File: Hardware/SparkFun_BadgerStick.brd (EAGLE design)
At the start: 17.8 x 66 mm, 39 parts, among them Q1 DMG2307L, U1 MIC5205-3.3V, U2 ATMEGA328P_TQFP, U3 CY7C65213, Y1 4MHz

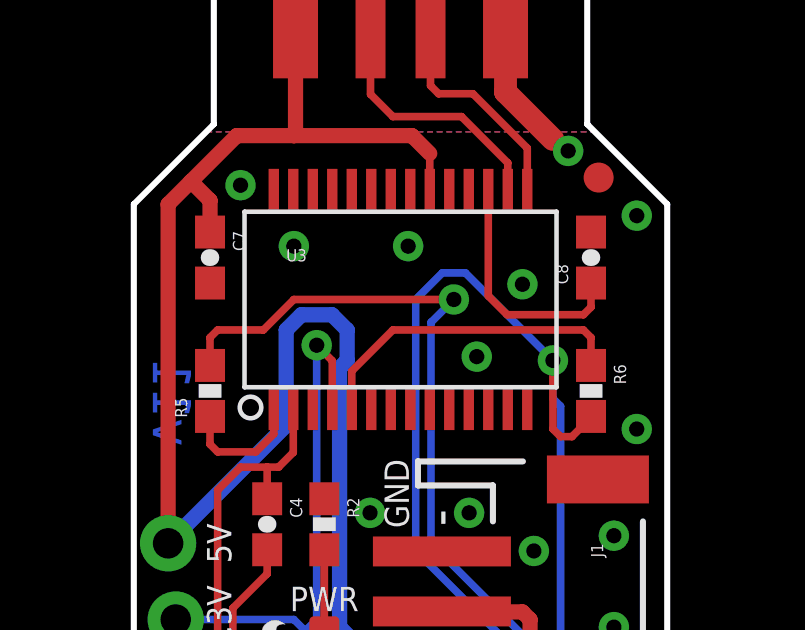
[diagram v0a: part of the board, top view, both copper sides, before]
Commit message: Switched Cypress USB-Serial bridge to FT232RL
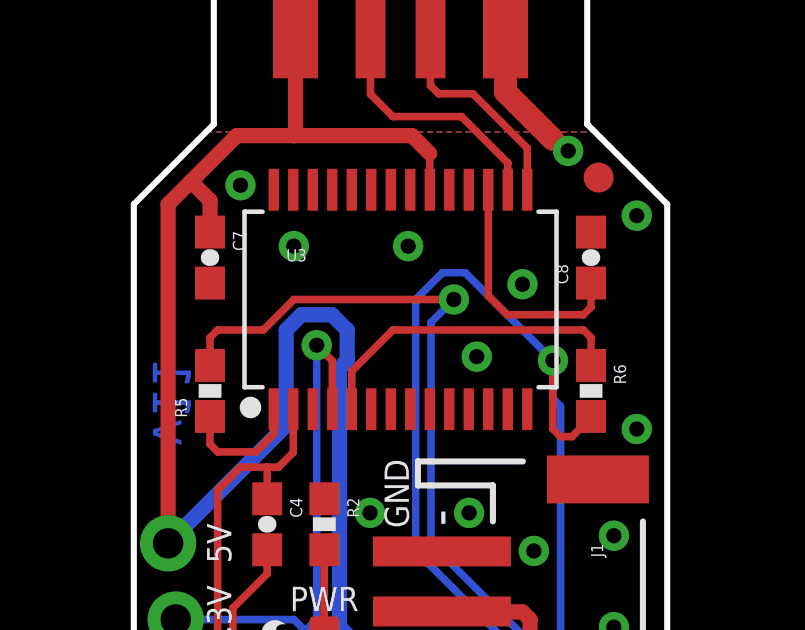
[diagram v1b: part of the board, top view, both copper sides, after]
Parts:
- U3: value CY7C65213 -> FT232RLSSOP
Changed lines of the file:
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@@
 <setting verticaltext="up"/>
 </settings>
-<grid distance="0.001" unitdist="inch" unit="inch" style="dots" multiple="1" display="yes" altdistance="0.0001" altunitdist="inch" altunit="inch"/>
+<grid distance="0.05" unitdist="inch" unit="inch" style="dots" multiple="1" display="yes" altdistance="0.005" altunitdist="inch" altunit="inch"/>
 <layers>
 <layer number="1" name="Top" color="4" fill="1" visible="yes" active="yes"/>
@@
 <layer number="45" name="Holes" color="7" fill="1" visible="yes" active="yes"/>
 <layer number="46" name="Milling" color="3" fill="1" visible="no" active="yes"/>
-<layer number="47" name="Measures" color="7" fill="1" visible="yes" active="yes"/>
+<layer number="47" name="Measures" color="7" fill="1" visible="no" active="yes"/>
 <layer number="51" name="tDocu" color="6" fill="1" visible="yes" active="yes"/>
 <layer number="52" name="bDocu" color="7" fill="1" visible="no" active="yes"/>
@@
 <attribute name="PROD_ID" value="IC-09069" x="8.89" y="19.05" size="1.778" layer="27" rot="R315" display="off"/>
 </element>
-<element name="U3" library="SparkFun-DigitalIC" package="SSOP28DB" value="CY7C65213" x="8.89" y="50.038">
-<attribute name="PROD_ID" value="IC-12487" x="8.89" y="50.038" size="1.778" layer="27" display="off"/>
+<element name="U3" library="SparkFun-DigitalIC" package="SSOP28DB" value="FT232RLSSOP" x="8.89" y="50.038">
+<attribute name="PROD_ID" value="IC-00870" x="8.89" y="50.038" size="1.778" layer="27" display="off"/>
 </element>
 <element name="JP6" library="SparkFun-Connectors" package="1X03_LOCK_NO_SILK" value="M03LOCK Female" x="6.35" y="1.27" smashed="yes">
